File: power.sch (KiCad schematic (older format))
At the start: 4 parts, among them J3 Conn_01x02_Male, J4 Conn_01x02_Male

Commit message: added TP4056 module
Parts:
- added C1: 1nF, Capacitor_SMD:C_0805_2012Metric_Pad1.15x1.40mm_HandSolder, symbol Device:C
- added D1: SM4007, Diode_SMD:D_MELF, symbol Diode:SM4007
- added F1: Fuse, Fuse:Fuse_1206_3216Metric, symbol Device:Fuse
- added R5: 806k, Resistor_SMD:R_0805_2012Metric_Pad1.15x1.40mm_HandSolder, symbol Device:R
- added R6: 2M, Resistor_SMD:R_0805_2012Metric_Pad1.15x1.40mm_HandSolder, symbol Device:R
- added U2: TP4056-module, Module:TP4056-module, symbol Power_Management:TP4056-module
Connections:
- net labels added: +BATT, GND, VBAT_ADC
- wire segments 0 -> 36
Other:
- note added: "Note:"
- note added: "TP4056 can charge two lipo cells (2S) in parallel but the voltage"
- note added: "Use a solar panel with output voltage between 4V to 8V"
- note added: "difference should not be greater then 0.2V to avoid balancing current!"
- moved on the sheet: BT1, BT2, J3, J4

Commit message: pcb layout
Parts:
- added C? (x2): 10uF, Capacitor_SMD:C_1210_3225Metric_Pad1.42x2.65mm_HandSolder, symbol Device:C
- added C?: 1nF, Capacitor_SMD:C_0805_2012Metric_Pad1.15x1.40mm_HandSolder, symbol Device:C
- added R?: 100k, Resistor_SMD:R_0805_2012Metric_Pad1.15x1.40mm_HandSolder, symbol Device:R
- added R? (x2): 2M, Resistor_SMD:R_0805_2012Metric_Pad1.15x1.40mm_HandSolder, symbol Device:R
- added SW?: SW_DPST_x2, Button_Switch_SMD:Panasonic_EVQPUL_EVQPUC, symbol Switch:SW_DPST_x2
- added U?: AP2112K-3.3, Package_TO_SOT_SMD:SOT-23-5, symbol Regulator_Linear:AP2112K-3.3
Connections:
- net labels added: +3.3V, VSOLAR, VSOLAR_ADC
- wire segments 36 -> 60
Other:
- note added: "TP4056 module schematic"
- note added: "https://learn.adafruit.com/assets/52793 dcdc design\n"
- moved on the sheet: BT1, BT2, C1, D1, F1, J3, J4, R5, R6

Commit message: created light control schematic
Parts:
- gave numbers to parts that had none: 8
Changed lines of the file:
@@
 $Descr A4 11693 8268
 encoding utf-8
-Sheet 4 4
+Sheet 4 5
 Title ""
 Date ""
@@
 VBAT_ADC
 $Comp
-L Regulator_Linear:AP2112K-3.3 U?
+L Regulator_Linear:AP2112K-3.3 U3
 U 1 1 5E7E7594
 P 5850 5100
-F 0 "U?" H 5850 5442 50  0000 C CNN
+F 0 "U3" H 5850 5442 50  0000 C CNN
 F 1 "AP2112K-3.3" H 5850 5351 50  0000 C CNN
 F 2 "Package_TO_SOT_SMD:SOT-23-5" H 5850 5425 50  0001 C CNN
@@
 $EndComp
 $Comp
-L power:GND #PWR?
+L power:GND #PWR0113
 U 1 1 5E7E7E11
 P 5850 5600
-F 0 "#PWR?" H 5850 5350 50  0001 C CNN
+F 0 "#PWR0113" H 5850 5350 50  0001 C CNN
 F 1 "GND" H 5855 5427 50  0000 C CNN
 F 2 "" H 5850 5600 50  0001 C CNN
@@
 	5850 5400 5850 5500
 $Comp
-L Device:C C?
+L Device:C C4
 U 1 1 5E7EB9D5
 P 6450 5150
-F 0 "C?" H 6565 5196 50  0000 L CNN
+F 0 "C4" H 6565 5196 50  0000 L CNN
 F 1 "10uF" H 6565 5105 50  0000 L CNN
 F 2 "Capacitor_SMD:C_1210_3225Metric_Pad1.42x2.65mm_HandSolder" H 6488 5000 50  0001 C CNN
@@
 $EndComp
 $Comp
-L Device:C C?
+L Device:C C3
 U 1 1 5E7EC1BF
 P 4700 5200
-F 0 "C?" H 4815 5246 50  0000 L CNN
+F 0 "C3" H 4815 5246 50  0000 L CNN
 F 1 "10uF" H 4815 5155 50  0000 L CNN
 F 2 "Capacitor_SMD:C_1210_3225Metric_Pad1.42x2.65mm_HandSolder" H 4738 5050 50  0001 C CNN
@@
 $EndComp
 $Comp
-L Device:R R?
+L Device:R R9
 U 1 1 5E7ECCE9
 P 5250 5100
-F 0 "R?" V 5150 5250 50  0000 C CNN
+F 0 "R9" V 5150 5250 50  0000 C CNN
 F 1 "100k" V 5150 5050 50  0000 C CNN
 F 2 "Resistor_SMD:R_0805_2012Metric_Pad1.15x1.40mm_HandSolder" V 5180 5100 50  0001 C CNN
@@
 Connection ~ 6450 5000
 $Comp
-L power:+3.3V #PWR?
+L power:+3.3V #PWR0114
 U 1 1 5E7F2BC0
 P 6450 4850
-F 0 "#PWR?" H 6450 4700 50  0001 C CNN
+F 0 "#PWR0114" H 6450 4700 50  0001 C CNN
 F 1 "+3.3V" H 6465 5023 50  0000 C CNN
 F 2 "" H 6450 4850 50  0001 C CNN
@@
 TP4056 module schematic
 $Comp
-L Device:C C?
+L Device:C C2
 U 1 1 5E817D9D
 P 1750 5850
-F 0 "C?" H 1865 5896 50  0000 L CNN
+F 0 "C2" H 1865 5896 50  0000 L CNN
 F 1 "1nF" H 1865 5805 50  0000 L CNN
 F 2 "Capacitor_SMD:C_0805_2012Metric_Pad1.15x1.40mm_HandSolder" H 1788 5700 50  0001 C CNN
@@
 $EndComp
 $Comp
-L power:GND #PWR?
+L power:GND #PWR0115
 U 1 1 5E817DA3
 P 2300 6100
-F 0 "#PWR?" H 2300 5850 50  0001 C CNN
+F 0 "#PWR0115" H 2300 5850 50  0001 C CNN
 F 1 "GND" H 2305 5927 50  0000 C CNN
 F 2 "" H 2300 6100 50  0001 C CNN
@@
 $EndComp
 $Comp
-L Device:R R?
+L Device:R R8
 U 1 1 5E817DA9
 P 2300 5850
-F 0 "R?" H 2370 5896 50  0000 L CNN
+F 0 "R8" H 2370 5896 50  0000 L CNN
 F 1 "2M" H 2370 5805 50  0000 L CNN
 F 2 "Resistor_SMD:R_0805_2012Metric_Pad1.15x1.40mm_HandSolder" V 2230 5850 50  0001 C CNN
@@
 VSOLAR_ADC
 $Comp
-L Device:R R?
+L Device:R R7
 U 1 1 5E81D1F8
 P 2300 5350
-F 0 "R?" H 2370 5396 50  0000 L CNN
+F 0 "R7" H 2370 5396 50  0000 L CNN
 F 1 "2M" H 2370 5305 50  0000 L CNN
 F 2 "Resistor_SMD:R_0805_2012Metric_Pad1.15x1.40mm_HandSolder" V 2230 5350 50  0001 C CNN
@@
 	2300 5000 2050 5000
 $Comp
-L Switch:SW_DPST_x2 SW?
+L Switch:SW_DPST_x2 SW1
 U 1 1 5E84363D
 P 5200 5800
-F 0 "SW?" H 5200 6035 50  0000 C CNN
+F 0 "SW1" H 5200 6035 50  0000 C CNN
 F 1 "SW_DPST_x2" H 5200 5944 50  0000 C CNN
 F 2 "Button_Switch_SMD:Panasonic_EVQPUL_EVQPUC" H 5200 5800 50  0001 C CNN

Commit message: layout
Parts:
- removed SW1: SW_DPST_x2, Button_Switch_SMD:Panasonic_EVQPUL_EVQPUC, symbol Switch:SW_DPST_x2
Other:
- note added: "Place switch to enable/disable\n"
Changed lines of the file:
@@
 Wire Wire Line
 	2300 5000 2050 5000
-$Comp
-L Switch:SW_DPST_x2 SW1
-U 1 1 5E84363D
-P 5200 5800
-F 0 "SW1" H 5200 6035 50  0000 C CNN
-F 1 "SW_DPST_x2" H 5200 5944 50  0000 C CNN
-F 2 "Button_Switch_SMD:Panasonic_EVQPUL_EVQPUC" H 5200 5800 50  0001 C CNN
-F 3 "~" H 5200 5800 50  0001 C CNN
-	1    5200 5800
-	1    0    0    -1
-$EndComp
+Text Notes 4450 4700 0    50   ~ 10
+Place switch to enable/disable\n
 $EndSCHEMATC

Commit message: added more circuit parts + new step files
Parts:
- added J8: Conn_01x02_Male, Connector_PinHeader_2.54mm:PinHeader_1x02_P2.54mm_Vertical, symbol Connector:Conn_01x02_Male
- added SW1: SW_Push_SPDT, Button_Switch_SMD:SW_SPDT_CK-JS102011SAQN, symbol Switch:SW_Push_SPDT
- J3, J4: footprint Connector_JST:JST_PH_S2B-PH-K_1x02_P2.00mm_Horizontal -> Connector_JST:JST_PH_S2B-PH-SM4-TB_1x02-1MP_P2.00mm_Horizontal
- U2: symbol Power_Management:TP4056-module -> inuk-base-rescue:TP4056-module-Power_Management
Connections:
- net labels added: EN, VIN
- wire segments 60 -> 65
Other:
- note added: "Place jumper or use switch to enable the system"
- note removed: "Place switch to enable/disable\n"
- moved on the sheet: R9

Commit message: started pcb routing
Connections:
- wire segments 65 -> 66
- no-connect marks 0 -> 1
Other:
- note added: "dcdc design based on https://learn.adafruit.com/assets/52793"
- note removed: "https://learn.adafruit.com/assets/52793 dcdc design\n"
- moved on the sheet: C2, C3, C4, D1, J4, J8, R7, R8, R9, SW1, U2, U3

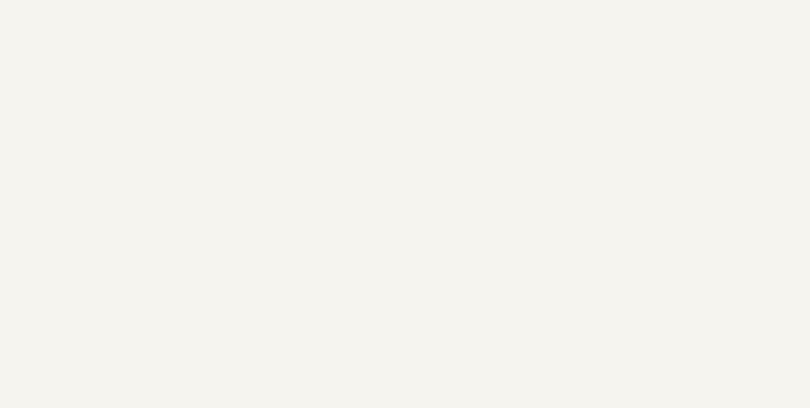
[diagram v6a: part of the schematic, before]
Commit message: layout and more silk informations
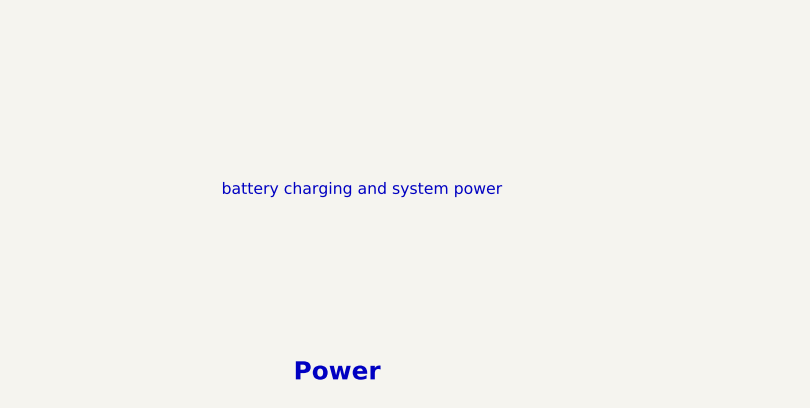
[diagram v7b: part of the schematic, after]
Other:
- note added: "Power"
- note added: "battery charging and system power"
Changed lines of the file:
@@
 	5600 6370 5950 6370
 NoConn ~ 5950 6370
+Text Notes 7365 7515 0    79   ~ 16
+Power
+Text Notes 7050 6700 0    50   ~ 0
+battery charging and system power
 $EndSCHEMATC

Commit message: finished layout, created production files and added readme
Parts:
- C1, C2: LCSC (none) -> C46653; MPN (none) -> CL21B102KBCNNNC
- C3, C4: LCSC (none) -> C13585; MPN (none) -> CL31A106KBHNNNE
- D1: value SM4007 -> B230-13-F; footprint Diode_SMD:D_MELF -> Diode_SMD:D_SMB; LCSC (none) -> C110482; MPN (none) -> B230-13-F
- F1: LCSC (none) -> C3105; MPN (none) -> 0466002.NRHF
- R5: LCSC (none) -> C63494; MPN (none) -> 0805W8F8063T5E
- R6, R7: LCSC (none) -> C26112; MPN (none) -> 0805W8F2004T5E
- R8: value 2M -> 806k; LCSC (none) -> C63494; MPN (none) -> 0805W8F8063T5E
- R9: LCSC (none) -> C17407; MPN (none) -> 0805W8F1003T5E
- U3: LCSC (none) -> C51118; MPN (none) -> AP2112K-3.3TRG1
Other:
- note added: "1.0"
- note added: "Place jumper or use switch to enable the system.\nThe LDO is disabled by default"
- note added: "To connect an external lipo"
- note added: "Use a solar panel with output voltage of 6V"
- note removed: "Place jumper or use switch to enable the system"
- note removed: "Use a solar panel with output voltage between 4V to 8V"
- note removed: "dcdc design based on https://learn.adafruit.com/assets/52793"
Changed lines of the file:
@@
 F 2 "Fuse:Fuse_1206_3216Metric" V 9180 1550 50  0001 C CNN
 F 3 "~" H 9250 1550 50  0001 C CNN
+F 4 "0466002.NRHF" H 9250 1550 50  0001 C CNN "MPN"
+F 5 "C3105" H 9250 1550 50  0001 C CNN "LCSC"
 	1    9250 1550
 	0    1    1    0
@@
 F 2 "Resistor_SMD:R_0805_2012Metric_Pad1.15x1.40mm_HandSolder" V 2480 1900 50  0001 C CNN
 F 3 "~" H 2550 1900 50  0001 C CNN
+F 4 "0805W8F8063T5E" H 2550 1900 50  0001 C CNN "MPN"
+F 5 "C63494" H 2550 1900 50  0001 C CNN "LCSC"
 	1    2550 1900
 	1    0    0    -1
@@
 F 2 "Capacitor_SMD:C_0805_2012Metric_Pad1.15x1.40mm_HandSolder" H 2038 2250 50  0001 C CNN
 F 3 "~" H 2000 2400 50  0001 C CNN
+F 4 "CL21B102KBCNNNC" H 2000 2400 50  0001 C CNN "MPN"
+F 5 "C46653" H 2000 2400 50  0001 C CNN "LCSC"
 	1    2000 2400
 	1    0    0    -1
@@
 F 2 "Resistor_SMD:R_0805_2012Metric_Pad1.15x1.40mm_HandSolder" V 2480 2400 50  0001 C CNN
 F 3 "~" H 2550 2400 50  0001 C CNN
+F 4 "0805W8F2004T5E" H 2550 2400 50  0001 C CNN "MPN"
+F 5 "C26112" H 2550 2400 50  0001 C CNN "LCSC"
 	1    2550 2400
 	1    0    0    -1
@@
 $EndComp
 Connection ~ 6450 4470
-Text Notes 4750 5620 0    50   ~ 0
-Place jumper or use switch to enable the system
-Text Notes 4750 5470 0    50   ~ 10
+Text Notes 4750 5550 0    50   ~ 0
+Place jumper or use switch to enable the system.\nThe LDO is disabled by default
+Text Notes 4750 5320 0    50   ~ 10
 Note:
 Wire Wire Line
@@
 F 2 "Resistor_SMD:R_0805_2012Metric_Pad1.15x1.40mm_HandSolder" V 5280 4770 50  0001 C CNN
 F 3 "~" H 5350 4770 50  0001 C CNN
+F 4 "0805W8F1003T5E" H 5350 4770 50  0001 C CNN "MPN"
+F 5 "C17407" H 5350 4770 50  0001 C CNN "LCSC"
 	1    5350 4770
 	1    0    0    -1
@@
 F 2 "Resistor_SMD:R_0805_2012Metric_Pad1.15x1.40mm_HandSolder" V 2230 4820 50  0001 C CNN
 F 3 "~" H 2300 4820 50  0001 C CNN
+F 4 "0805W8F2004T5E" H 2300 4820 50  0001 C CNN "MPN"
+F 5 "C26112" H 2300 4820 50  0001 C CNN "LCSC"
 	1    2300 4820
 	1    0    0    -1
@@
 	2300 4970 2300 5070
 $Comp
-L Device:R R8
-U 1 1 5E817DA9
-P 2300 5320
-F 0 "R8" H 2370 5366 50  0000 L CNN
-F 1 "2M" H 2370 5275 50  0000 L CNN
-F 2 "Resistor_SMD:R_0805_2012Metric_Pad1.15x1.40mm_HandSolder" V 2230 5320 50  0001 C CNN
-F 3 "~" H 2300 5320 50  0001 C CNN
-	1    2300 5320
-	1    0    0    -1
-$EndComp
-$Comp
 L power:GND #PWR0115
 U 1 1 5E817DA3
@@
 F 2 "Capacitor_SMD:C_0805_2012Metric_Pad1.15x1.40mm_HandSolder" H 1788 5170 50  0001 C CNN
 F 3 "~" H 1750 5320 50  0001 C CNN
+F 4 "CL21B102KBCNNNC" H 1750 5320 50  0001 C CNN "MPN"
+F 5 "C46653" H 1750 5320 50  0001 C CNN "LCSC"
 	1    1750 5320
 	1    0    0    -1
@@
 Wire Wire Line
 	4700 4470 3950 4470
-Text Notes 4150 3970 0    50   ~ 0
-dcdc design based on https://learn.adafruit.com/assets/52793
 Wire Wire Line
 	4700 4470 4700 4520
@@
 F 2 "Capacitor_SMD:C_1210_3225Metric_Pad1.42x2.65mm_HandSolder" H 4738 4520 50  0001 C CNN
 F 3 "~" H 4700 4670 50  0001 C CNN
+F 4 "CL31A106KBHNNNE" H 4700 4670 50  0001 C CNN "MPN"
+F 5 "C13585" H 4700 4670 50  0001 C CNN "LCSC"
 	1    4700 4670
 	1    0    0    -1
@@
 F 2 "Capacitor_SMD:C_1210_3225Metric_Pad1.42x2.65mm_HandSolder" H 6488 4470 50  0001 C CNN
 F 3 "~" H 6450 4620 50  0001 C CNN
+F 4 "CL31A106KBHNNNE" H 6450 4620 50  0001 C CNN "MPN"
+F 5 "C13585" H 6450 4620 50  0001 C CNN "LCSC"
 	1    6450 4620
 	1    0    0    -1
@@
 F 2 "Package_TO_SOT_SMD:SOT-23-5" H 5850 4895 50  0001 C CNN
 F 3 "https://www.diodes.com/assets/Datasheets/AP2112.pdf" H 5850 4670 50  0001 C CNN
+F 4 "AP2112K-3.3TRG1" H 5850 4570 50  0001 C CNN "MPN"
+F 5 "C51118" H 5850 4570 50  0001 C CNN "LCSC"
 	1    5850 4570
 	1    0    0    -1
 $EndComp
 Text Notes 1200 3970 0    50   ~ 0
-Use a solar panel with output voltage between 4V to 8V
+Use a solar panel with output voltage of 6V
 Text Notes 1200 3820 0    50   ~ 10
 Note:
@@
 P 1900 4470
 F 0 "D1" H 1900 4254 50  0000 C CNN
-F 1 "SM4007" H 1900 4345 50  0000 C CNN
-F 2 "Diode_SMD:D_MELF" H 1900 4346 50  0001 C CNN
+F 1 "B230-13-F" H 1900 4345 50  0000 C CNN
+F 2 "Diode_SMD:D_SMB" H 1900 4346 50  0001 C CNN
 F 3 "http://cdn-reichelt.de/documents/datenblatt/A400/SMD1N400%23DIO.pdf" H 1900 4470 50  0001 C CNN
+F 4 "B230-13-F" H 1900 4470 50  0001 C CNN "MPN"
+F 5 " C110482" H 1900 4470 50  0001 C CNN "LCSC"
 	1    1900 4470
 	-1   0    0    1
@@
 Text Notes 7050 6700 0    50   ~ 0
 battery charging and system power
+Text Notes 9850 1870 0    50   ~ 0
+To connect an external lipo
+$Comp
+L Device:R R8
+U 1 1 5EA0530B
+P 2300 5320
+F 0 "R8" H 2370 5366 50  0000 L CNN
+F 1 "806k" H 2370 5275 50  0000 L CNN
+F 2 "Resistor_SMD:R_0805_2012Metric_Pad1.15x1.40mm_HandSolder" V 2230 5320 50  0001 C CNN
+F 3 "~" H 2300 5320 50  0001 C CNN
+F 4 "0805W8F8063T5E" H 2300 5320 50  0001 C CNN "MPN"
+F 5 "C63494" H 2300 5320 50  0001 C CNN "LCSC"
+	1    2300 5320
+	1    0    0    -1
+$EndComp
+Text Notes 10590 7640 0    50   ~ 0
+1.0
 $EndSCHEMATC
